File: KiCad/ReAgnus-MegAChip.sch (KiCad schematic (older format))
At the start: 36 parts, among them J3 Conn_02x01, J4 Conn_01x01, J5 Conn_01x01, J6 Conn_01x01, J7 Conn_01x01, U1 PLCC-84-Plug, U2 LM1117-3.3, U3 SN74CBTD16210, U4 SN74CBTD16210, U5 SN74CBTD16210, U6 SN74CBTD16210, U8 74LVC1G07, U9 Agnus_TH_plug_pins

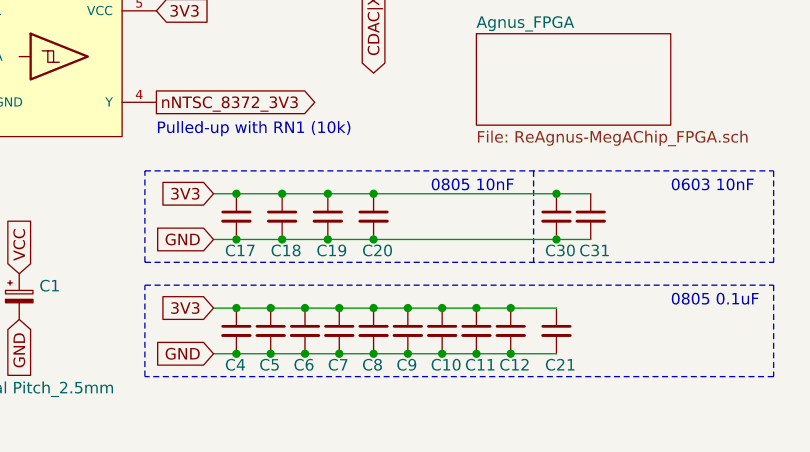
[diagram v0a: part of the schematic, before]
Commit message: fixed power routing and decoupling caps for U10 (SDRAM)
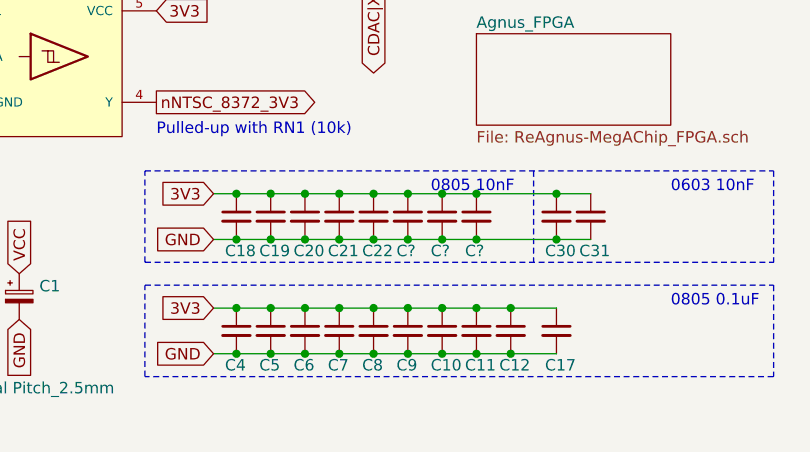
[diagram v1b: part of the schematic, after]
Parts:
- added C22, C? (x3): 0.01uF, Capacitor_SMD:C_0805_2012Metric_Pad1.15x1.40mm_HandSolder, symbol Device:C_Small
- renumbered C21 to C17, C17 to C18, C18 to C19, C19 to C20, C20 to C21
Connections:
- wire segments 57 -> 65
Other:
- moved on the sheet: C19, C20, C21
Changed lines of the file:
@@
 Pulled-up with RN1 (10k)
 $Comp
-L Device:C_Small C18
+L Device:C_Small C19
 U 1 1 6333CF1B
-P 4600 6950
-AR Path="/6333CF1B" Ref="C18"  Part="1"
+P 4550 6950
+AR Path="/6333CF1B" Ref="C19"  Part="1"
 AR Path="/632D3BDF/6333CF1B" Ref="C?"  Part="1"
 AR Path="/632F104D/6333CF1B" Ref="C?"  Part="1"
-F 0 "C18" H 4550 6800 50  0000 L CNN
-F 1 "0.01uF" H 4550 6700 50  0001 L CNN
-F 2 "Capacitor_SMD:C_0805_2012Metric_Pad1.15x1.40mm_HandSolder" H 4600 6950 50  0001 C CNN
-F 3 "~" H 4600 6950 50  0001 C CNN
-	1    4600 6950
+F 0 "C19" H 4500 6800 50  0000 L CNN
+F 1 "0.01uF" H 4500 6700 50  0001 L CNN
+F 2 "Capacitor_SMD:C_0805_2012Metric_Pad1.15x1.40mm_HandSolder" H 4550 6950 50  0001 C CNN
+F 3 "~" H 4550 6950 50  0001 C CNN
+	1    4550 6950
 	1    0    0    -1
 $EndComp
@@
 $EndComp
 Wire Wire Line
-	4400 6850 4600 6850
+	4400 6850 4550 6850
 Connection ~ 4400 6850
 Wire Wire Line
-	4400 7050 4600 7050
+	4400 7050 4550 7050
 Connection ~ 4400 7050
-Connection ~ 4600 6850
-Connection ~ 4600 7050
 Text GLabel 3450 7400 3    50   Input ~ 0
 GND
@@
 Wire Notes Line
 	4000 6750 6750 6750
-Wire Wire Line
-	4600 6850 4800 6850
-Wire Wire Line
-	4600 7050 4800 7050
 Text Notes 6300 6850 0    50   ~ 0
 0603 10nF
@@
 $EndComp
 $Comp
-L Device:C_Small C17
+L Device:C_Small C18
 U 1 1 63302CD2
 P 4400 6950
-AR Path="/63302CD2" Ref="C17"  Part="1"
+AR Path="/63302CD2" Ref="C18"  Part="1"
 AR Path="/632D3BDF/63302CD2" Ref="C?"  Part="1"
 AR Path="/632F104D/63302CD2" Ref="C?"  Part="1"
-F 0 "C17" H 4350 6800 50  0000 L CNN
+F 0 "C18" H 4350 6800 50  0000 L CNN
 F 1 "0.01uF" H 4400 6700 50  0001 L CNN
 F 2 "Capacitor_SMD:C_0805_2012Metric_Pad1.15x1.40mm_HandSolder" H 4400 6950 50  0001 C CNN
@@
 Connection ~ 5450 7550
 $Comp
-L Device:C_Small C19
+L Device:C_Small C20
 U 1 1 63426A79
-P 4800 6950
-AR Path="/63426A79" Ref="C19"  Part="1"
+P 4700 6950
+AR Path="/63426A79" Ref="C20"  Part="1"
 AR Path="/632D3BDF/63426A79" Ref="C?"  Part="1"
 AR Path="/632F104D/63426A79" Ref="C?"  Part="1"
-F 0 "C19" H 4750 6800 50  0000 L CNN
-F 1 "0.01uF" H 4750 6700 50  0001 L CNN
-F 2 "Capacitor_SMD:C_0805_2012Metric_Pad1.15x1.40mm_HandSolder" H 4800 6950 50  0001 C CNN
-F 3 "~" H 4800 6950 50  0001 C CNN
-	1    4800 6950
-	1    0    0    -1
-$EndComp
-Connection ~ 4800 6850
-Wire Wire Line
-	4800 6850 5000 6850
-Connection ~ 4800 7050
-Wire Wire Line
-	4800 7050 5000 7050
-$Comp
-L Device:C_Small C20
+F 0 "C20" H 4650 6800 50  0000 L CNN
+F 1 "0.01uF" H 4650 6700 50  0001 L CNN
+F 2 "Capacitor_SMD:C_0805_2012Metric_Pad1.15x1.40mm_HandSolder" H 4700 6950 50  0001 C CNN
+F 3 "~" H 4700 6950 50  0001 C CNN
+	1    4700 6950
+	1    0    0    -1
+$EndComp
+$Comp
+L Device:C_Small C21
 U 1 1 6370FC11
-P 5000 6950
-AR Path="/6370FC11" Ref="C20"  Part="1"
+P 4850 6950
+AR Path="/6370FC11" Ref="C21"  Part="1"
 AR Path="/632D3BDF/6370FC11" Ref="C?"  Part="1"
 AR Path="/632F104D/6370FC11" Ref="C?"  Part="1"
-F 0 "C20" H 4950 6800 50  0000 L CNN
+F 0 "C21" H 4800 6800 50  0000 L CNN
+F 1 "0.01uF" H 4800 6700 50  0001 L CNN
+F 2 "Capacitor_SMD:C_0805_2012Metric_Pad1.15x1.40mm_HandSolder" H 4850 6950 50  0001 C CNN
+F 3 "~" H 4850 6950 50  0001 C CNN
+	1    4850 6950
+	1    0    0    -1
+$EndComp
+$Comp
+L Device:C_Small C17
+U 1 1 638ABF1F
+P 5800 7450
+AR Path="/638ABF1F" Ref="C17"  Part="1"
+AR Path="/632D3BDF/638ABF1F" Ref="C?"  Part="1"
+AR Path="/632F104D/638ABF1F" Ref="C?"  Part="1"
+F 0 "C17" H 5750 7300 50  0000 L CNN
+F 1 "0.1uF" H 5800 7200 50  0001 L CNN
+F 2 "Capacitor_SMD:C_0805_2012Metric_Pad1.15x1.40mm_HandSolder" H 5800 7450 50  0001 C CNN
+F 3 "~" H 5800 7450 50  0001 C CNN
+	1    5800 7450
+	1    0    0    -1
+$EndComp
+Wire Wire Line
+	5600 7350 5800 7350
+Connection ~ 5600 7350
+Wire Wire Line
+	5600 7550 5800 7550
+Connection ~ 5600 7550
+$Comp
+L Device:C_Small C22
+U 1 1 638B9A03
+P 5000 6950
+AR Path="/638B9A03" Ref="C22"  Part="1"
+AR Path="/632D3BDF/638B9A03" Ref="C?"  Part="1"
+AR Path="/632F104D/638B9A03" Ref="C?"  Part="1"
+F 0 "C22" H 4950 6800 50  0000 L CNN
 F 1 "0.01uF" H 4950 6700 50  0001 L CNN
 F 2 "Capacitor_SMD:C_0805_2012Metric_Pad1.15x1.40mm_HandSolder" H 5000 6950 50  0001 C CNN
@@
 	1    0    0    -1
 $EndComp
+$Comp
+L Device:C_Small C?
+U 1 1 638CDBEE
+P 5150 6950
+AR Path="/638CDBEE" Ref="C?"  Part="1"
+AR Path="/632D3BDF/638CDBEE" Ref="C?"  Part="1"
+AR Path="/632F104D/638CDBEE" Ref="C?"  Part="1"
+F 0 "C?" H 5100 6800 50  0000 L CNN
+F 1 "0.01uF" H 5100 6700 50  0001 L CNN
+F 2 "Capacitor_SMD:C_0805_2012Metric_Pad1.15x1.40mm_HandSolder" H 5150 6950 50  0001 C CNN
+F 3 "~" H 5150 6950 50  0001 C CNN
+	1    5150 6950
+	1    0    0    -1
+$EndComp
+Connection ~ 4550 6850
+Connection ~ 4550 7050
+Connection ~ 4700 6850
+Connection ~ 4700 7050
+Wire Wire Line
+	4550 6850 4700 6850
+Wire Wire Line
+	4550 7050 4700 7050
+Wire Wire Line
+	4700 6850 4850 6850
+Wire Wire Line
+	4700 7050 4850 7050
+Connection ~ 4850 6850
+Connection ~ 4850 7050
+Wire Wire Line
+	4850 6850 5000 6850
+Wire Wire Line
+	4850 7050 5000 7050
 Connection ~ 5000 6850
-Wire Wire Line
-	5000 6850 5800 6850
 Connection ~ 5000 7050
 Wire Wire Line
-	5000 7050 5800 7050
-$Comp
-L Device:C_Small C21
-U 1 1 638ABF1F
-P 5800 7450
-AR Path="/638ABF1F" Ref="C21"  Part="1"
-AR Path="/632D3BDF/638ABF1F" Ref="C?"  Part="1"
-AR Path="/632F104D/638ABF1F" Ref="C?"  Part="1"
-F 0 "C21" H 5750 7300 50  0000 L CNN
-F 1 "0.1uF" H 5800 7200 50  0001 L CNN
-F 2 "Capacitor_SMD:C_0805_2012Metric_Pad1.15x1.40mm_HandSolder" H 5800 7450 50  0001 C CNN
-F 3 "~" H 5800 7450 50  0001 C CNN
-	1    5800 7450
-	1    0    0    -1
-$EndComp
-Wire Wire Line
-	5600 7350 5800 7350
-Connection ~ 5600 7350
-Wire Wire Line
-	5600 7550 5800 7550
-Connection ~ 5600 7550
+	5000 6850 5150 6850
+Wire Wire Line
+	5000 7050 5150 7050
+Connection ~ 5150 6850
+Connection ~ 5150 7050
+Wire Wire Line
+	5150 6850 5300 6850
+Wire Wire Line
+	5150 7050 5300 7050
+$Comp
+L Device:C_Small C?
+U 1 1 638D832C
+P 5300 6950
+AR Path="/638D832C" Ref="C?"  Part="1"
+AR Path="/632D3BDF/638D832C" Ref="C?"  Part="1"
+AR Path="/632F104D/638D832C" Ref="C?"  Part="1"
+F 0 "C?" H 5250 6800 50  0000 L CNN
+F 1 "0.01uF" H 5250 6700 50  0001 L CNN
+F 2 "Capacitor_SMD:C_0805_2012Metric_Pad1.15x1.40mm_HandSolder" H 5300 6950 50  0001 C CNN
+F 3 "~" H 5300 6950 50  0001 C CNN
+	1    5300 6950
+	1    0    0    -1
+$EndComp
+Connection ~ 5300 6850
+Wire Wire Line
+	5300 6850 5450 6850
+Connection ~ 5300 7050
+Wire Wire Line
+	5300 7050 5450 7050
+$Comp
+L Device:C_Small C?
+U 1 1 638D8E59
+P 5450 6950
+AR Path="/638D8E59" Ref="C?"  Part="1"
+AR Path="/632D3BDF/638D8E59" Ref="C?"  Part="1"
+AR Path="/632F104D/638D8E59" Ref="C?"  Part="1"
+F 0 "C?" H 5400 6800 50  0000 L CNN
+F 1 "0.01uF" H 5400 6700 50  0001 L CNN
+F 2 "Capacitor_SMD:C_0805_2012Metric_Pad1.15x1.40mm_HandSolder" H 5450 6950 50  0001 C CNN
+F 3 "~" H 5450 6950 50  0001 C CNN
+	1    5450 6950
+	1    0    0    -1
+$EndComp
+Connection ~ 5450 6850
+Wire Wire Line
+	5450 6850 5800 6850
+Connection ~ 5450 7050
+Wire Wire Line
+	5450 7050 5800 7050
 $EndSCHEMATC

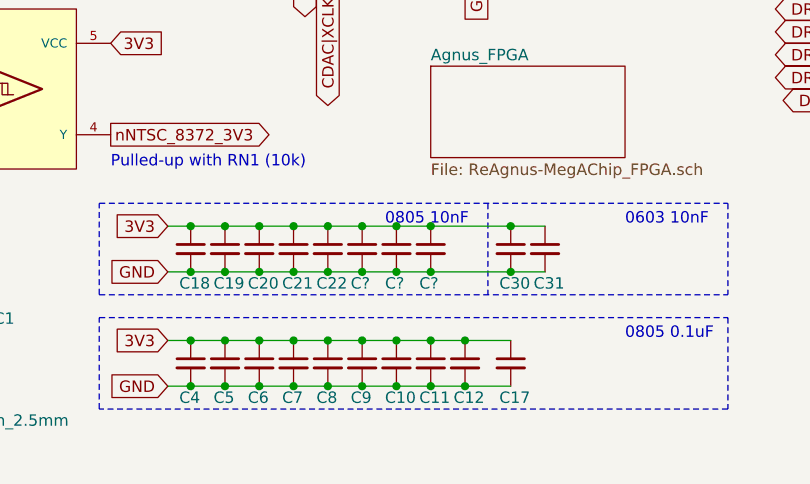
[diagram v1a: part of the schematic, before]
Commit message: fixed power routing and decoupling caps for U10 (SDRAM)
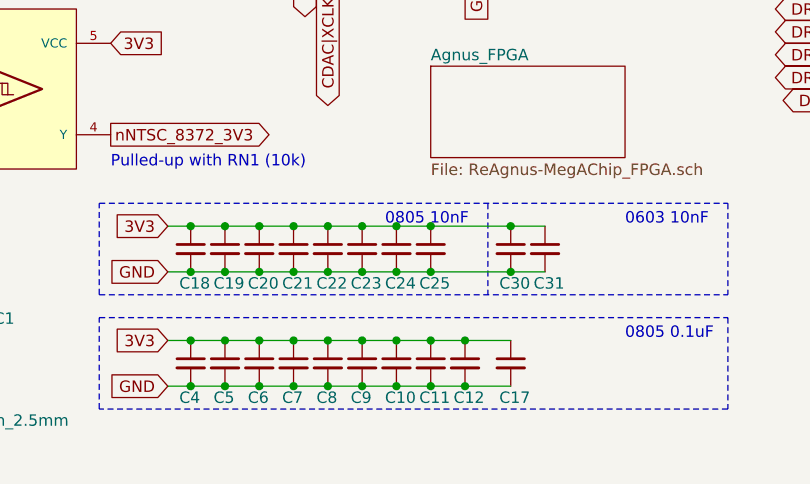
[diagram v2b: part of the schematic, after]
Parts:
- gave numbers to parts that had none: 3
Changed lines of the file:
@@
 $EndComp
 $Comp
-L Device:C_Small C?
+L Device:C_Small C23
 U 1 1 638CDBEE
 P 5150 6950
-AR Path="/638CDBEE" Ref="C?"  Part="1"
+AR Path="/638CDBEE" Ref="C23"  Part="1"
 AR Path="/632D3BDF/638CDBEE" Ref="C?"  Part="1"
 AR Path="/632F104D/638CDBEE" Ref="C?"  Part="1"
-F 0 "C?" H 5100 6800 50  0000 L CNN
+F 0 "C23" H 5100 6800 50  0000 L CNN
 F 1 "0.01uF" H 5100 6700 50  0001 L CNN
 F 2 "Capacitor_SMD:C_0805_2012Metric_Pad1.15x1.40mm_HandSolder" H 5150 6950 50  0001 C CNN
@@
 	5150 7050 5300 7050
 $Comp
-L Device:C_Small C?
+L Device:C_Small C24
 U 1 1 638D832C
 P 5300 6950
-AR Path="/638D832C" Ref="C?"  Part="1"
+AR Path="/638D832C" Ref="C24"  Part="1"
 AR Path="/632D3BDF/638D832C" Ref="C?"  Part="1"
 AR Path="/632F104D/638D832C" Ref="C?"  Part="1"
-F 0 "C?" H 5250 6800 50  0000 L CNN
+F 0 "C24" H 5250 6800 50  0000 L CNN
 F 1 "0.01uF" H 5250 6700 50  0001 L CNN
 F 2 "Capacitor_SMD:C_0805_2012Metric_Pad1.15x1.40mm_HandSolder" H 5300 6950 50  0001 C CNN
@@
 	5300 7050 5450 7050
 $Comp
-L Device:C_Small C?
+L Device:C_Small C25
 U 1 1 638D8E59
 P 5450 6950
-AR Path="/638D8E59" Ref="C?"  Part="1"
+AR Path="/638D8E59" Ref="C25"  Part="1"
 AR Path="/632D3BDF/638D8E59" Ref="C?"  Part="1"
 AR Path="/632F104D/638D8E59" Ref="C?"  Part="1"
-F 0 "C?" H 5400 6800 50  0000 L CNN
+F 0 "C25" H 5400 6800 50  0000 L CNN
 F 1 "0.01uF" H 5400 6700 50  0001 L CNN
 F 2 "Capacitor_SMD:C_0805_2012Metric_Pad1.15x1.40mm_HandSolder" H 5450 6950 50  0001 C CNN

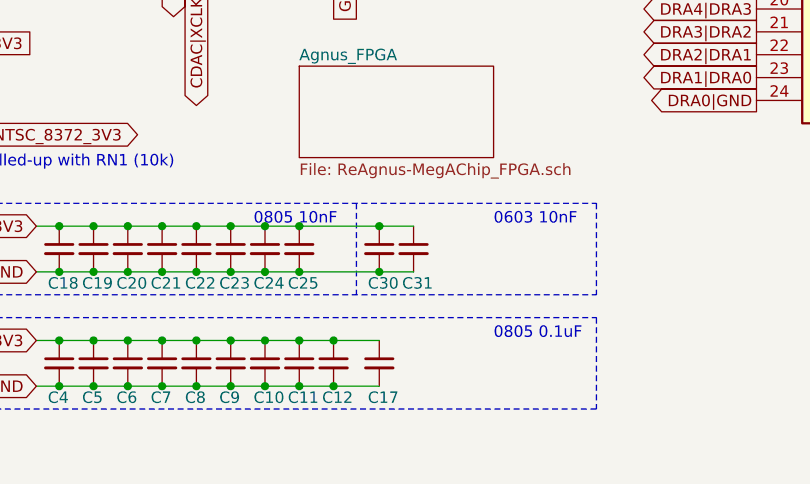
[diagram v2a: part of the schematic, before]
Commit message: silkscreen fixes
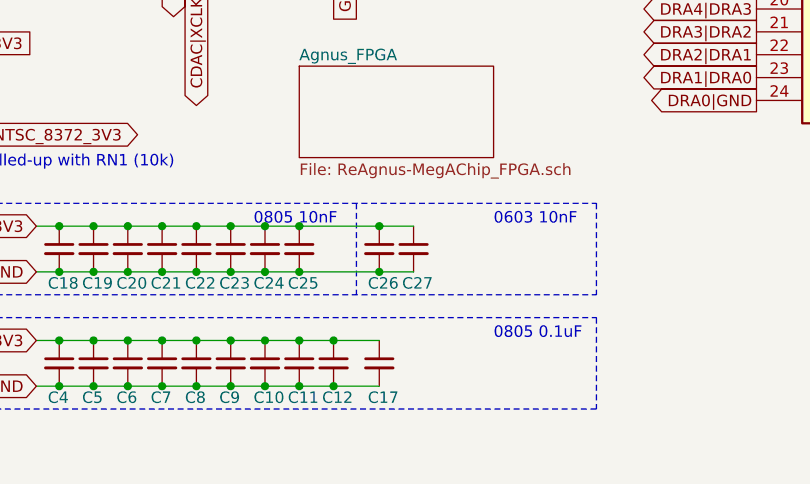
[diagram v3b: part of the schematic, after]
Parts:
- renumbered C30 to C26, C31 to C27
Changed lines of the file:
@@
 GND
 $Comp
-L Device:C_Small C30
+L Device:C_Small C26
 U 1 1 631E37EB
 P 5800 6950
-AR Path="/631E37EB" Ref="C30"  Part="1"
+AR Path="/631E37EB" Ref="C26"  Part="1"
 AR Path="/632D3BDF/631E37EB" Ref="C?"  Part="1"
 AR Path="/632F104D/631E37EB" Ref="C?"  Part="1"
-F 0 "C30" H 5750 6800 50  0000 L CNN
+F 0 "C26" H 5750 6800 50  0000 L CNN
 F 1 "0.01uF" H 5550 6900 50  0001 L CNN
 F 2 "Capacitor_SMD:C_0603_1608Metric_Pad1.05x0.95mm_HandSolder" H 5800 6950 50  0001 C CNN
@@
 	4300 6850 4400 6850
 $Comp
-L Device:C_Small C31
+L Device:C_Small C27
 U 1 1 632C350C
 P 5950 6950
-AR Path="/632C350C" Ref="C31"  Part="1"
+AR Path="/632C350C" Ref="C27"  Part="1"
 AR Path="/632D3BDF/632C350C" Ref="C?"  Part="1"
 AR Path="/632F104D/632C350C" Ref="C?"  Part="1"
-F 0 "C31" H 5900 6800 50  0000 L CNN
+F 0 "C27" H 5900 6800 50  0000 L CNN
 F 1 "0.01uF" H 5900 6700 50  0001 L CNN
 F 2 "Capacitor_SMD:C_0603_1608Metric_Pad1.05x0.95mm_HandSolder" H 5950 6950 50  0001 C CNN

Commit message: Added JP3 with pull-up resistor on FPGA-pin IOL5A to J3-jack and changed J3 from a two- to a three-pinHeader.
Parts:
- removed J3: Conn_02x01, Connector_PinHeader_2.54mm:PinHeader_2x01_P2.54mm_Vertical, symbol Connector_Generic:Conn_02x01
- added J3: Conn_01x03, Connector_PinHeader_2.54mm:PinHeader_1x03_P2.54mm_Vertical, symbol Connector_Generic:Conn_01x03
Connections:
- net labels added: JP3
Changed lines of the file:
@@
 NoConn ~ 650  6500
 NoConn ~ 650  6650
-$Comp
-L Connector_Generic:Conn_02x01 J3
-U 1 1 60E54D12
-P 1900 6650
-F 0 "J3" H 1950 6867 50  0000 C CNN
-F 1 "Conn_02x01" H 1950 6776 50  0000 C CNN
-F 2 "Connector_PinHeader_2.54mm:PinHeader_2x01_P2.54mm_Vertical" H 1900 6650 50  0001 C CNN
-F 3 "~" H 1900 6650 50  0001 C CNN
-	1    1900 6650
-	1    0    0    -1
-$EndComp
-Text GLabel 2200 6650 2    50   Input ~ 0
+Text GLabel 2000 6550 3    50   Input ~ 0
 GND
 Wire Wire Line
@@
 Text GLabel 1700 7300 0    50   Input ~ 0
 VCC
-Text GLabel 1700 6650 0    50   Input ~ 0
+Text GLabel 1900 6550 3    50   Input ~ 0
 VCC
 Text GLabel 1850 7100 1    50   Input ~ 0
@@
 Wire Wire Line
 	5450 7050 5800 7050
+Text GLabel 2100 6550 3    50   Input ~ 0
+JP3
+$Comp
+L Connector_Generic:Conn_01x03 J3
+U 1 1 63977F90
+P 2000 6350
+F 0 "J3" V 1964 6162 50  0000 R CNN
+F 1 "Conn_01x03" V 1873 6162 50  0000 R CNN
+F 2 "Connector_PinHeader_2.54mm:PinHeader_1x03_P2.54mm_Vertical" H 2000 6350 50  0001 C CNN
+F 3 "~" H 2000 6350 50  0001 C CNN
+	1    2000 6350
+	0    -1   -1   0
+$EndComp
 $EndSCHEMATC
